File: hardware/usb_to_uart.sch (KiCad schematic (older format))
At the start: 4 parts

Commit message: update cp2102,
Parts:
- added C?: C106,0603, Capacitor_SMD:C_0603_1608Metric_Pad1.05x0.95mm_HandSolder, symbol taobao-c:C106,0603
- added C?: C104,0603, Capacitor_SMD:C_0603_1608Metric_Pad1.05x0.95mm_HandSolder, symbol taobao-c:C104,0603
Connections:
- net GND: now also C?.2, C?.2
- net ACTIVE: now reaches U?.11 (~SUSPEND~)
- net CTS: now reaches U?.23 (CTS)
- net RTS: now reaches U?.24 (RTS)
- net TXD0: now reaches U?.25 (RXD)
- net +5V: now reaches U?.8 (VBUS)
- net +5V: now also C?.1, C?.1
- net RXD0: now reaches R?.1
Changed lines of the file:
@@
 	1800 3850 1700 3850
 Connection ~ 1700 3850
+$Comp
+L power:+5V #PWR?
+U 1 1 5CD65D2C
+P 3200 4400
+F 0 "#PWR?" H 3200 4250 50  0001 C CNN
+F 1 "+5V" H 3250 4600 50  0000 C CNN
+F 2 "" H 3200 4400 50  0001 C CNN
+F 3 "" H 3200 4400 50  0001 C CNN
+	1    3200 4400
+	1    0    0    -1
+$EndComp
+$Comp
+L taobao-c:C106,0603 C?
+U 1 1 5CD6621A
+P 3200 4750
+F 0 "C?" H 3100 4800 50  0000 R CNN
+F 1 "C106,0603" H 3100 4750 50  0000 R CNN
+F 2 "Capacitor_SMD:C_0603_1608Metric_Pad1.05x0.95mm_HandSolder" H 3200 4750 50  0001 C CNN
+F 3 "~" H 3200 4750 50  0001 C CNN
+	1    3200 4750
+	1    0    0    -1
+$EndComp
+$Comp
+L taobao-c:C104,0603 C?
+U 1 1 5CD66224
+P 3450 4750
+F 0 "C?" H 3550 4800 50  0000 L CNN
+F 1 "C104,0603" H 3550 4750 50  0000 L CNN
+F 2 "Capacitor_SMD:C_0603_1608Metric_Pad1.05x0.95mm_HandSolder" H 3450 4750 50  0001 C CNN
+F 3 "~" H 3450 4750 50  0001 C CNN
+	1    3450 4750
+	1    0    0    -1
+$EndComp
+Wire Wire Line
+	3700 4000 3700 4500
+Wire Wire Line
+	3700 4500 3450 4500
+Wire Wire Line
+	3200 4500 3200 4650
+Wire Wire Line
+	3200 4400 3200 4500
+Connection ~ 3200 4500
+Wire Wire Line
+	3450 4500 3450 4650
+Connection ~ 3450 4500
+Wire Wire Line
+	3450 4500 3200 4500
+$Comp
+L power:GND #PWR?
+U 1 1 5CD68920
+P 3350 5050
+F 0 "#PWR?" H 3350 4800 50  0001 C CNN
+F 1 "GND" H 3400 4850 50  0000 C CNN
+F 2 "" H 3350 5050 50  0001 C CNN
+F 3 "" H 3350 5050 50  0001 C CNN
+	1    3350 5050
+	1    0    0    -1
+$EndComp
+Wire Wire Line
+	3200 4850 3200 4950
+Wire Wire Line
+	3200 4950 3350 4950
+Wire Wire Line
+	3350 4950 3350 5050
+Wire Wire Line
+	3450 4850 3450 4950
+Wire Wire Line
+	3450 4950 3350 4950
+Connection ~ 3350 4950
+Text Label 4000 4450 1    50   ~ 0
+ACTIVE
+Wire Wire Line
+	4000 4000 4000 4450
+Text Label 4150 1550 3    50   ~ 0
+RTS
+Text Label 4250 1550 3    50   ~ 0
+CTS
+Wire Wire Line
+	4150 1550 4150 2000
+Wire Wire Line
+	4250 1550 4250 2000
+Text Label 4650 1400 2    50   ~ 0
+TXD0
+Text Label 4650 1300 2    50   ~ 0
+RXD0
+Wire Wire Line
+	4650 1300 4300 1300
+Wire Wire Line
+	4650 1400 4050 1400
+Wire Wire Line
+	4050 1400 4050 2000
 $EndSCHEMATC

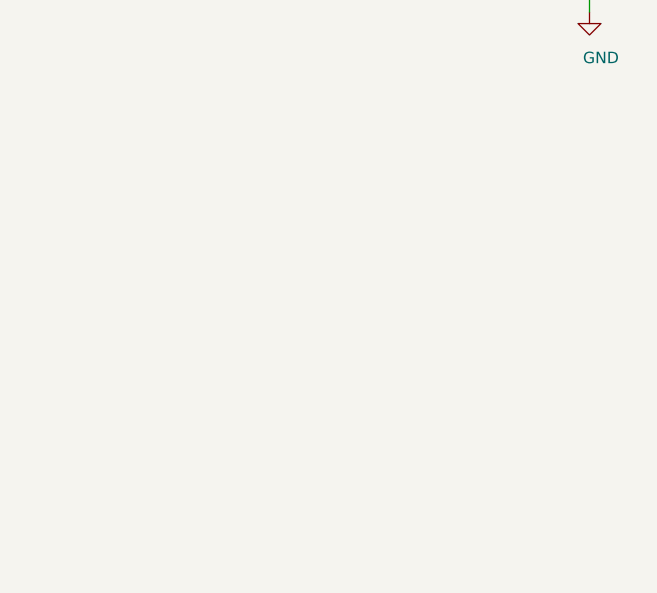
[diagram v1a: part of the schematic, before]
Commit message: update usb to uart,
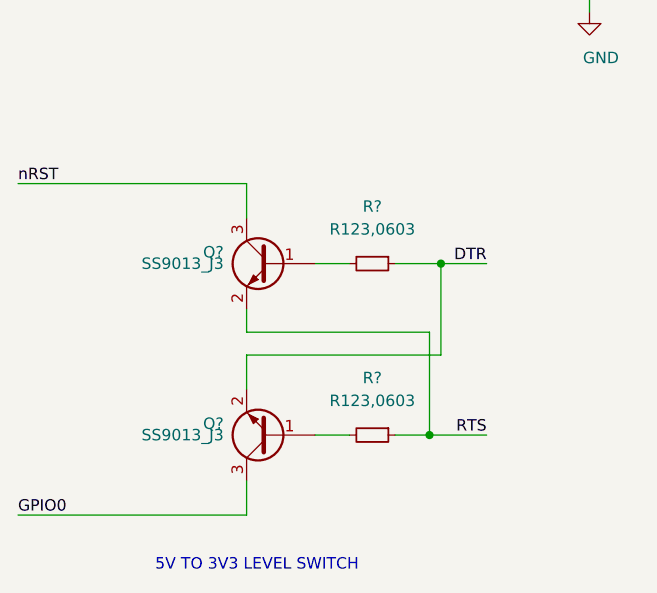
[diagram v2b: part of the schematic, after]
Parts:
- added Q? (x2): SS9013_J3, footprint-lib:9013,J3,SOT23, symbol taobao-transistor:SS9013_J3
- added R? (x2): R123,0603, Resistor_SMD:R_0603_1608Metric_Pad1.05x0.95mm_HandSolder, symbol taobao-r:R123,0603
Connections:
- net DTR: now also Q?.2 (E), R?.1
- net RTS: now also Q?.2 (E), R?.1
- new net: Q?.1 (B), R?.2 (x2)
- new net GPIO0: Q?.3 (C)
- new net nRST: Q?.3 (C)
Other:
- note added: "5V TO 3V3 LEVEL SWITCH"
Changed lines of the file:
@@
 Wire Wire Line
 	4050 1400 4050 2000
+$Comp
+L taobao-transistor:SS9013_J3 Q?
+U 1 1 5CD7BF83
+P 1950 6150
+F 0 "Q?" H 2150 6200 50  0000 L CNN
+F 1 "SS9013_J3" H 2150 6150 50  0000 L CNN
+F 2 "footprint-lib:9013,J3,SOT23" H 2150 6075 50  0001 L CIN
+F 3 "https://www.fairchildsemi.com/datasheets/2N/2N3904.pdf" H 1950 6150 50  0001 L CNN
+	1    1950 6150
+	-1   0    0    -1
+$EndComp
+$Comp
+L taobao-transistor:SS9013_J3 Q?
+U 1 1 5CD7C99C
+P 1950 6900
+F 0 "Q?" H 2150 6850 50  0000 L CNN
+F 1 "SS9013_J3" H 2150 6900 50  0000 L CNN
+F 2 "footprint-lib:9013,J3,SOT23" H 2150 6825 50  0001 L CIN
+F 3 "https://www.fairchildsemi.com/datasheets/2N/2N3904.pdf" H 1950 6900 50  0001 L CNN
+	1    1950 6900
+	-1   0    0    1
+$EndComp
+Text Label 850  5800 0    50   ~ 0
+nRST
+Text Label 850  7250 0    50   ~ 0
+GPIO0
+Text Label 2900 6150 2    50   ~ 0
+DTR
+Text Label 2900 6900 2    50   ~ 0
+RTS
+Wire Wire Line
+	850  5800 1850 5800
+Wire Wire Line
+	1850 5800 1850 5950
+Wire Wire Line
+	850  7250 1850 7250
+Wire Wire Line
+	1850 7250 1850 7100
+Wire Wire Line
+	1850 6350 1850 6450
+Wire Wire Line
+	1850 6450 2650 6450
+Wire Wire Line
+	2650 6450 2650 6900
+Wire Wire Line
+	2650 6900 2900 6900
+$Comp
+L taobao-r:R123,0603 R?
+U 1 1 5CD7F8D4
+P 2400 6150
+F 0 "R?" V 2150 6150 50  0000 C CNN
+F 1 "R123,0603" V 2250 6150 50  0000 C CNN
+F 2 "Resistor_SMD:R_0603_1608Metric_Pad1.05x0.95mm_HandSolder" H 2400 6150 50  0001 C CNN
+F 3 "~" H 2400 6150 50  0001 C CNN
+	1    2400 6150
+	0    1    1    0
+$EndComp
+$Comp
+L taobao-r:R123,0603 R?
+U 1 1 5CD7FB22
+P 2400 6900
+F 0 "R?" V 2150 6900 50  0000 C CNN
+F 1 "R123,0603" V 2250 6900 50  0000 C CNN
+F 2 "Resistor_SMD:R_0603_1608Metric_Pad1.05x0.95mm_HandSolder" H 2400 6900 50  0001 C CNN
+F 3 "~" H 2400 6900 50  0001 C CNN
+	1    2400 6900
+	0    1    1    0
+$EndComp
+Wire Wire Line
+	2150 6150 2300 6150
+Wire Wire Line
+	2500 6150 2700 6150
+Wire Wire Line
+	2150 6900 2300 6900
+Wire Wire Line
+	2500 6900 2650 6900
+Connection ~ 2650 6900
+Wire Wire Line
+	1850 6700 1850 6550
+Wire Wire Line
+	1850 6550 2700 6550
+Wire Wire Line
+	2700 6550 2700 6150
+Connection ~ 2700 6150
+Wire Wire Line
+	2700 6150 2900 6150
+Text Notes 1450 7500 0    50   ~ 0
+5V TO 3V3 LEVEL SWITCH
 $EndSCHEMATC

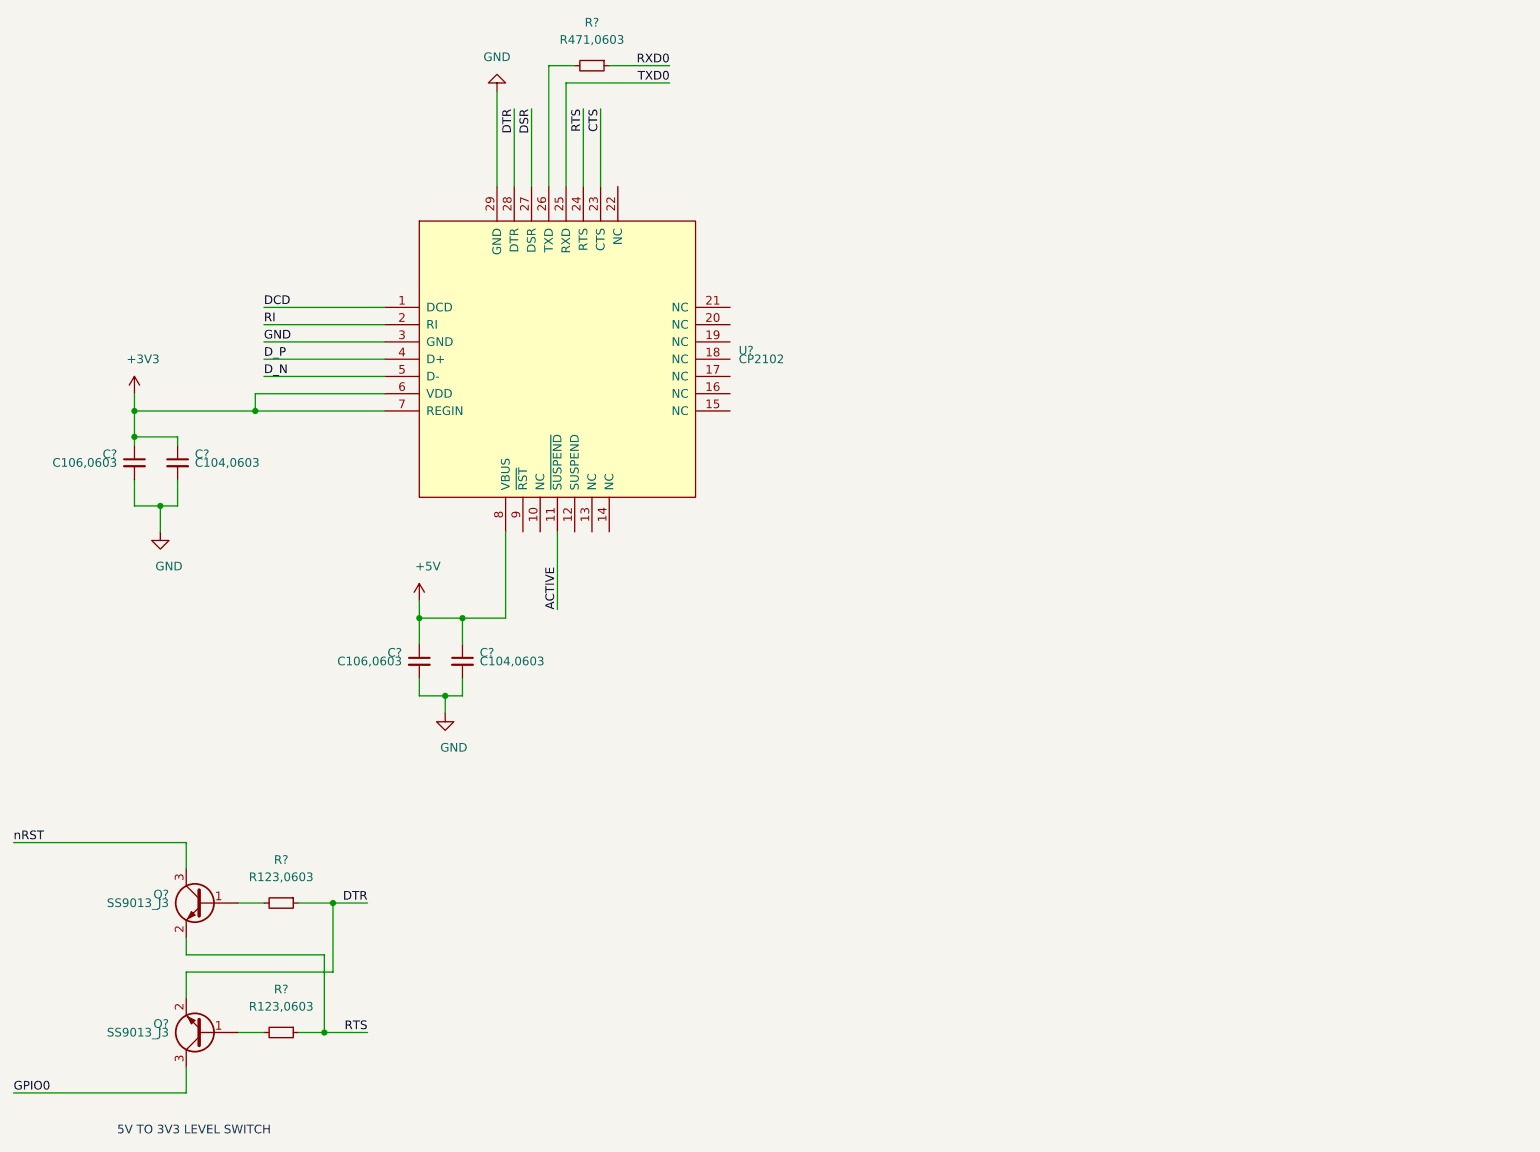
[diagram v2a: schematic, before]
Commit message: update usb to uart,
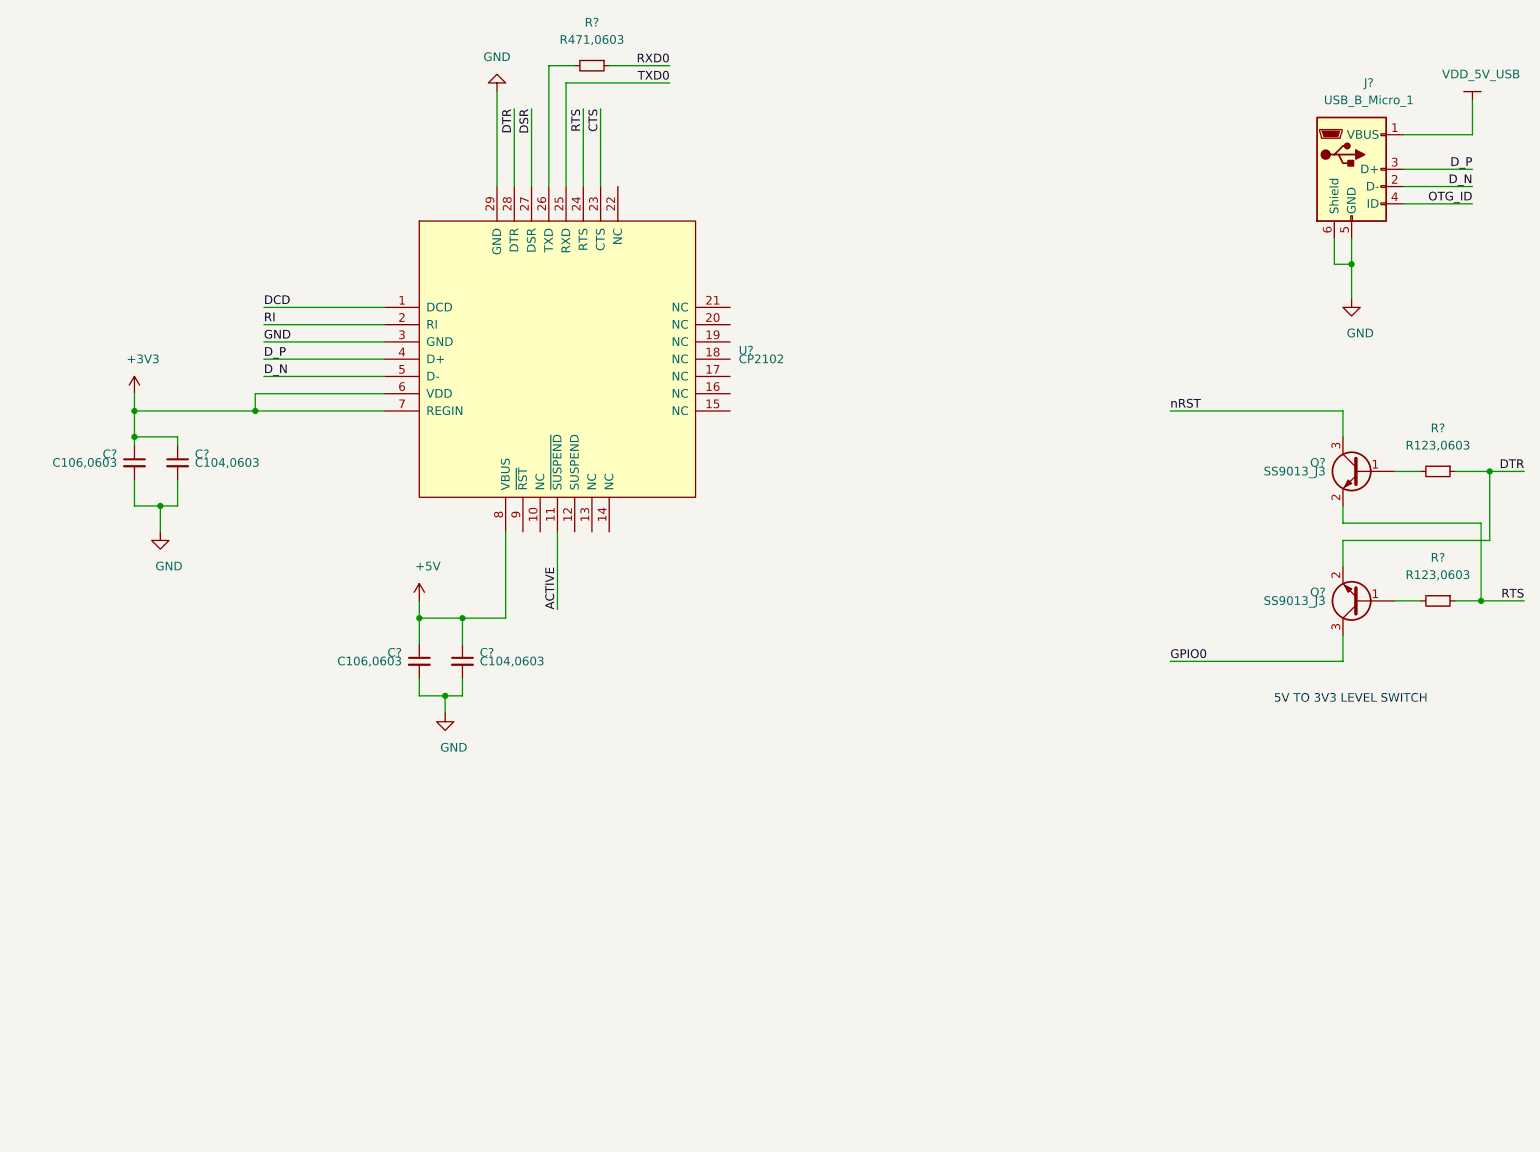
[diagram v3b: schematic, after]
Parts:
- added J?: USB_B_Micro_1, footprint-lib:USB_Micro-B_Molex-105017-0001, symbol taobao-components:USB_B_Micro_1
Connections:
- net D_N: now also J?.2 (D-)
- net D_P: now also J?.3 (D+)
- net GND: now also J?.5 (GND), J?.6 (Shield)
- new net OTG_ID: J?.4 (ID)
- new net VDD_5V_USB: J?.1 (VBUS)
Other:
- moved on the sheet: Q?, R?
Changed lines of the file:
@@
 L taobao-transistor:SS9013_J3 Q?
 U 1 1 5CD7BF83
-P 1950 6150
-F 0 "Q?" H 2150 6200 50  0000 L CNN
-F 1 "SS9013_J3" H 2150 6150 50  0000 L CNN
-F 2 "footprint-lib:9013,J3,SOT23" H 2150 6075 50  0001 L CIN
-F 3 "https://www.fairchildsemi.com/datasheets/2N/2N3904.pdf" H 1950 6150 50  0001 L CNN
-	1    1950 6150
+P 8650 3650
+F 0 "Q?" H 8850 3700 50  0000 L CNN
+F 1 "SS9013_J3" H 8850 3650 50  0000 L CNN
+F 2 "footprint-lib:9013,J3,SOT23" H 8850 3575 50  0001 L CIN
+F 3 "https://www.fairchildsemi.com/datasheets/2N/2N3904.pdf" H 8650 3650 50  0001 L CNN
+	1    8650 3650
 	-1   0    0    -1
 $EndComp
@@
 L taobao-transistor:SS9013_J3 Q?
 U 1 1 5CD7C99C
-P 1950 6900
-F 0 "Q?" H 2150 6850 50  0000 L CNN
-F 1 "SS9013_J3" H 2150 6900 50  0000 L CNN
-F 2 "footprint-lib:9013,J3,SOT23" H 2150 6825 50  0001 L CIN
-F 3 "https://www.fairchildsemi.com/datasheets/2N/2N3904.pdf" H 1950 6900 50  0001 L CNN
-	1    1950 6900
+P 8650 4400
+F 0 "Q?" H 8850 4350 50  0000 L CNN
+F 1 "SS9013_J3" H 8850 4400 50  0000 L CNN
+F 2 "footprint-lib:9013,J3,SOT23" H 8850 4325 50  0001 L CIN
+F 3 "https://www.fairchildsemi.com/datasheets/2N/2N3904.pdf" H 8650 4400 50  0001 L CNN
+	1    8650 4400
 	-1   0    0    1
 $EndComp
-Text Label 850  5800 0    50   ~ 0
+Text Label 7550 3300 0    50   ~ 0
 nRST
-Text Label 850  7250 0    50   ~ 0
+Text Label 7550 4750 0    50   ~ 0
 GPIO0
-Text Label 2900 6150 2    50   ~ 0
+Text Label 9600 3650 2    50   ~ 0
 DTR
-Text Label 2900 6900 2    50   ~ 0
+Text Label 9600 4400 2    50   ~ 0
 RTS
 Wire Wire Line
-	850  5800 1850 5800
+	7550 3300 8550 3300
 Wire Wire Line
-	1850 5800 1850 5950
+	8550 3300 8550 3450
 Wire Wire Line
-	850  7250 1850 7250
+	7550 4750 8550 4750
 Wire Wire Line
-	1850 7250 1850 7100
+	8550 4750 8550 4600
 Wire Wire Line
-	1850 6350 1850 6450
+	8550 3850 8550 3950
 Wire Wire Line
-	1850 6450 2650 6450
+	8550 3950 9350 3950
 Wire Wire Line
-	2650 6450 2650 6900
+	9350 3950 9350 4400
 Wire Wire Line
-	2650 6900 2900 6900
+	9350 4400 9600 4400
 $Comp
 L taobao-r:R123,0603 R?
 U 1 1 5CD7F8D4
-P 2400 6150
-F 0 "R?" V 2150 6150 50  0000 C CNN
-F 1 "R123,0603" V 2250 6150 50  0000 C CNN
-F 2 "Resistor_SMD:R_0603_1608Metric_Pad1.05x0.95mm_HandSolder" H 2400 6150 50  0001 C CNN
-F 3 "~" H 2400 6150 50  0001 C CNN
-	1    2400 6150
+P 9100 3650
+F 0 "R?" V 8850 3650 50  0000 C CNN
+F 1 "R123,0603" V 8950 3650 50  0000 C CNN
+F 2 "Resistor_SMD:R_0603_1608Metric_Pad1.05x0.95mm_HandSolder" H 9100 3650 50  0001 C CNN
+F 3 "~" H 9100 3650 50  0001 C CNN
+	1    9100 3650
 	0    1    1    0
 $EndComp
@@
 L taobao-r:R123,0603 R?
 U 1 1 5CD7FB22
-P 2400 6900
-F 0 "R?" V 2150 6900 50  0000 C CNN
-F 1 "R123,0603" V 2250 6900 50  0000 C CNN
-F 2 "Resistor_SMD:R_0603_1608Metric_Pad1.05x0.95mm_HandSolder" H 2400 6900 50  0001 C CNN
-F 3 "~" H 2400 6900 50  0001 C CNN
-	1    2400 6900
+P 9100 4400
+F 0 "R?" V 8850 4400 50  0000 C CNN
+F 1 "R123,0603" V 8950 4400 50  0000 C CNN
+F 2 "Resistor_SMD:R_0603_1608Metric_Pad1.05x0.95mm_HandSolder" H 9100 4400 50  0001 C CNN
+F 3 "~" H 9100 4400 50  0001 C CNN
+	1    9100 4400
 	0    1    1    0
 $EndComp
 Wire Wire Line
-	2150 6150 2300 6150
+	8850 3650 9000 3650
 Wire Wire Line
-	2500 6150 2700 6150
+	9200 3650 9400 3650
 Wire Wire Line
-	2150 6900 2300 6900
+	8850 4400 9000 4400
 Wire Wire Line
-	2500 6900 2650 6900
-Connection ~ 2650 6900
+	9200 4400 9350 4400
+Connection ~ 9350 4400
 Wire Wire Line
-	1850 6700 1850 6550
+	8550 4200 8550 4050
 Wire Wire Line
-	1850 6550 2700 6550
+	8550 4050 9400 4050
 Wire Wire Line
-	2700 6550 2700 6150
-Connection ~ 2700 6150
+	9400 4050 9400 3650
+Connection ~ 9400 3650
 Wire Wire Line
-	2700 6150 2900 6150
-Text Notes 1450 7500 0    50   ~ 0
+	9400 3650 9600 3650
+Text Notes 8150 5000 0    50   ~ 0
 5V TO 3V3 LEVEL SWITCH
+$Comp
+L taobao-components:USB_B_Micro_1 J?
+U 1 1 5CD480A9
+P 8600 1900
+F 0 "J?" H 8700 2400 50  0000 C CNN
+F 1 "USB_B_Micro_1" H 8700 2300 50  0000 C CNN
+F 2 "footprint-lib:USB_Micro-B_Molex-105017-0001" H 8600 900 50  0001 C CNN
+F 3 "~" H 8750 1850 50  0001 C CNN
+	1    8600 1900
+	1    0    0    -1
+$EndComp
+$Comp
+L power:GND #PWR?
+U 1 1 5CD48A65
+P 8600 2650
+F 0 "#PWR?" H 8600 2400 50  0001 C CNN
+F 1 "GND" H 8650 2450 50  0000 C CNN
+F 2 "" H 8600 2650 50  0001 C CNN
+F 3 "" H 8600 2650 50  0001 C CNN
+	1    8600 2650
+	1    0    0    -1
+$EndComp
+Wire Wire Line
+	8500 2300 8500 2450
+Wire Wire Line
+	8500 2450 8600 2450
+Wire Wire Line
+	8600 2450 8600 2650
+Wire Wire Line
+	8600 2300 8600 2450
+Connection ~ 8600 2450
+Wire Wire Line
+	9300 1500 9300 1700
+Wire Wire Line
+	9300 1700 8900 1700
+Text Label 9300 1900 2    50   ~ 0
+D_P
+Text Label 9300 2000 2    50   ~ 0
+D_N
+Text Label 9300 2100 2    50   ~ 0
+OTG_ID
+Wire Wire Line
+	9300 1900 8900 1900
+Wire Wire Line
+	9300 2000 8900 2000
+Wire Wire Line
+	9300 2100 8900 2100
+$Comp
+L taobao-components:VDD_5V_USB #PWR?
+U 1 1 5CD693FB
+P 9300 1500
+F 0 "#PWR?" H 9300 1350 50  0001 C CNN
+F 1 "VDD_5V_USB" H 9350 1650 50  0000 C CNN
+F 2 "" H 9300 1500 50  0001 C CNN
+F 3 "" H 9300 1500 50  0001 C CNN
+	1    9300 1500
+	1    0    0    -1
+$EndComp
 $EndSCHEMATC
